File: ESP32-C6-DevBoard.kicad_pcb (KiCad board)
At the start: 2 copper layers, 63.5 x 30.5 mm, 46 parts, among them J1 USB_C_Receptacle_USB2.0_16P, J2 Conn_01x10_Pin, J3 Conn_01x10_Pin, J4 USB_C_Receptacle_USB2.0_16P, Q1 BC847, Q2 BC847, SW1 SW_Push_Dual, SW2 SW_Push_Dual, U1 ESP32-C6-MINI-1, U2 CP2104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

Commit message: First version done without autorouter.
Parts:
- removed J3: Conn_01x10_Pin, Connector_PinHeader_2.54mm:PinHeader_1x10_P2.54mm_Vertical
- removed R16: 470, Resistor_SMD:R_0603_1608Metric
- removed SW1, SW2: SW_Push_Dual, TS04_66_55_BK_260_SMT:SW_TS04-66-55-BK-260-SMT
- removed U4, U5: USBLC6-2SC6, Package_TO_SOT_SMD:SOT-23-6
- added D10: SD05_SOD323, Diode_SMD:D_SOD-323, F.Cu at (99.1, 72.4)
- added D11: SD05_SOD323, Diode_SMD:D_SOD-323, F.Cu at (100.3, 67.3)
- added D12: SD05_SOD323, Diode_SMD:D_SOD-323, F.Cu at (102.9, 72.4)
- added D8: SD05_SOD323, Diode_SMD:D_SOD-323, F.Cu at (102.9, 52.1)
- added D9: SD05_SOD323, Diode_SMD:D_SOD-323, F.Cu at (99.1, 54.6)
- added J5: Conn_01x16_Pin, Connector_PinHeader_2.54mm:PinHeader_1x16_P2.54mm_Vertical, F.Cu at (106.7, 74.9)
- added J6: Conn_01x16_Pin, Connector_PinHeader_2.54mm:PinHeader_1x16_P2.54mm_Vertical, F.Cu at (106.7, 54.6)
- added S1: TS-1088-AR02016, TS-1088-AR02016:SW_TS-1088-AR02016, F.Cu at (125.7, 59.7)
- added S2: TS-1088-AR02016, TS-1088-AR02016:SW_TS-1088-AR02016, F.Cu at (125.7, 67.3)
- C5: value 0.1uF -> 1.0uF
- D6: value LED -> SD05_SOD323; footprint LED_SMD:LED_0603_1608Metric -> Diode_SMD:D_SOD-323
- J2: value Conn_01x10_Pin -> Conn_01x02_Pin; footprint Connector_PinHeader_2.54mm:PinHeader_1x10_P2.54mm_Vertical -> Connector_PinHeader_2.54mm:PinHeader_1x02_P2.54mm_Vertical; moved to F.Cu
- moved J2 38.3 mm to (107.7, 59.3), turned to 0 degrees
- moved U3 33.0 mm to (99.1, 62.2), turned to 180 degrees
- moved D1 29.7 mm to (104.1, 59.7)
- moved R5 28.2 mm to (104.1, 62.2), turned to 0 degrees
- moved R4 25.5 mm to (101.6, 62.2), turned to 90 degrees
- moved C2 23.2 mm to (104.1, 64.8)
- moved C8 22.0 mm to (109.8, 68.6), turned to -90 degrees
- moved R3 21.6 mm to (100.3, 64.8), turned to 180 degrees
- moved C3 17.1 mm to (120.7, 67.3)
- moved C1 16.9 mm to (143.5, 57.1), turned to 0 degrees
- moved C9 15.3 mm to (111.5, 68.6), turned to -90 degrees
- moved R10 12.7 mm to (118.1, 58.4)
- moved U2 12.5 mm to (115.6, 67.3)
- moved R9 11.4 mm to (118.1, 63.5)
- moved R12 10.2 mm to (108.0, 68.6), turned to -90 degrees
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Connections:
- net /USB1_VBUS renamed /PWR_USB1_VBUS
- net /USB_5V renamed /PWR_5V
- net Net-(Q1-C) renamed /RTS
- net Net-(Q2-C) renamed /DTR
- C1 pad 1: /3V3 -> /PWR_3V3
- C2 pad 1: /3V3 -> Net-(J2-Pin_2)
- C4 pad 1: /3V3 -> /PWR_3V3
- C8 pad 1: /3V3 -> /PWR_3V3
- C9 pad 1: /3V3 -> /PWR_3V3
- D2 pad 2: /USB2_VBUS -> /PWR_USB2_VBUS
- D6 pad 2: Net-(D6-A) -> /PWR_USB2_VBUS
- J1 pad A6: Net-(J1-D+-PadA6) -> /USB1_P
- J1 pad A7: Net-(J1-D--PadA7) -> /USB1_N
- J1 pad B6: Net-(J1-D+-PadA6) -> /USB1_P
- J1 pad B7: Net-(J1-D--PadA7) -> /USB1_N
- J2 pad 1: /EIO0 -> /PWR_3V3
- J2 pad 2: /EIO1 -> Net-(J2-Pin_2)
- J4 pad A4: /USB2_VBUS -> /PWR_USB2_VBUS
- J4 pad A6: Net-(J4-D+-PadA6) -> /USB2_P
- J4 pad A7: Net-(J4-D--PadA7) -> /USB2_N
- J4 pad A9: /USB2_VBUS -> /PWR_USB2_VBUS
- J4 pad B4: /USB2_VBUS -> /PWR_USB2_VBUS
- J4 pad B6: Net-(J4-D+-PadA6) -> /USB2_P
- J4 pad B7: Net-(J4-D--PadA7) -> /USB2_N
- J4 pad B9: /USB2_VBUS -> /PWR_USB2_VBUS
- R12 pad 1: /3V3 -> /PWR_3V3
- R15 pad 1: /USB2_VBUS -> /PWR_USB2_VBUS
- R3 pad 1: /3V3 -> Net-(J2-Pin_2)
- R5 pad 1: /3V3 -> Net-(J2-Pin_2)
- R6 pad 1: /3V3 -> /PWR_3V3
- U1 pad 3: /3V3 -> /PWR_3V3
- U2 pad 5: /3V3 -> /PWR_3V3
- U2 pad 6: /3V3 -> /PWR_3V3
- U2 pad 7: /3V3 -> /PWR_3V3
- U2 pad 8: /USB2_VBUS -> /PWR_USB2_VBUS
- U3 pad 1: /3V3 -> Net-(J2-Pin_2)
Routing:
- net GND: track 313.4 -> 34.1 mm, vias 0 -> 23
- net /3V3: track 93.6 -> 0.00 mm, vias 4 -> 0
- net /PWR_3V3: track 0.00 -> 66.4 mm, vias 0 -> 2
- net /EIO0: track 61.6 -> 12.6 mm, vias 2 -> 0
- net /PWR_USB2_VBUS: track 0.00 -> 48.7 mm, vias 0 -> 2
- net /CHIP_PU: track 65.1 -> 25.0 mm, vias 2 -> 3
- net /PWR_5V: track 70.4 -> 32.3 mm, vias 3 -> 2
- net /USB2_VBUS: track 37.0 -> 0.00 mm, vias 2 -> 0
- net /ERXD0: track 51.7 -> 27.3 mm, vias 1 -> 2
- net /EIO8: track 22.8 -> 0.00 mm, vias 1 -> 0
- net /ETXD0: track 50.3 -> 28.9 mm, vias 1 -> 2
- net /EIO1: track 15.8 -> 35.2 mm
- net Net-(J4-D--PadA7): track 17.8 -> 0.00 mm, vias 2 -> 0
- net /EIO4: track 9.78 -> 26.7 mm, vias 0 -> 1
- net /USB2_N: track 16.9 -> 33.6 mm, vias 2 -> 0
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- added copper zone on B.Cu, net GND
- added copper zone on F.Cu, net GND
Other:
- board text removed: "Ekmansoft"
- board text removed: "KenTroniq"

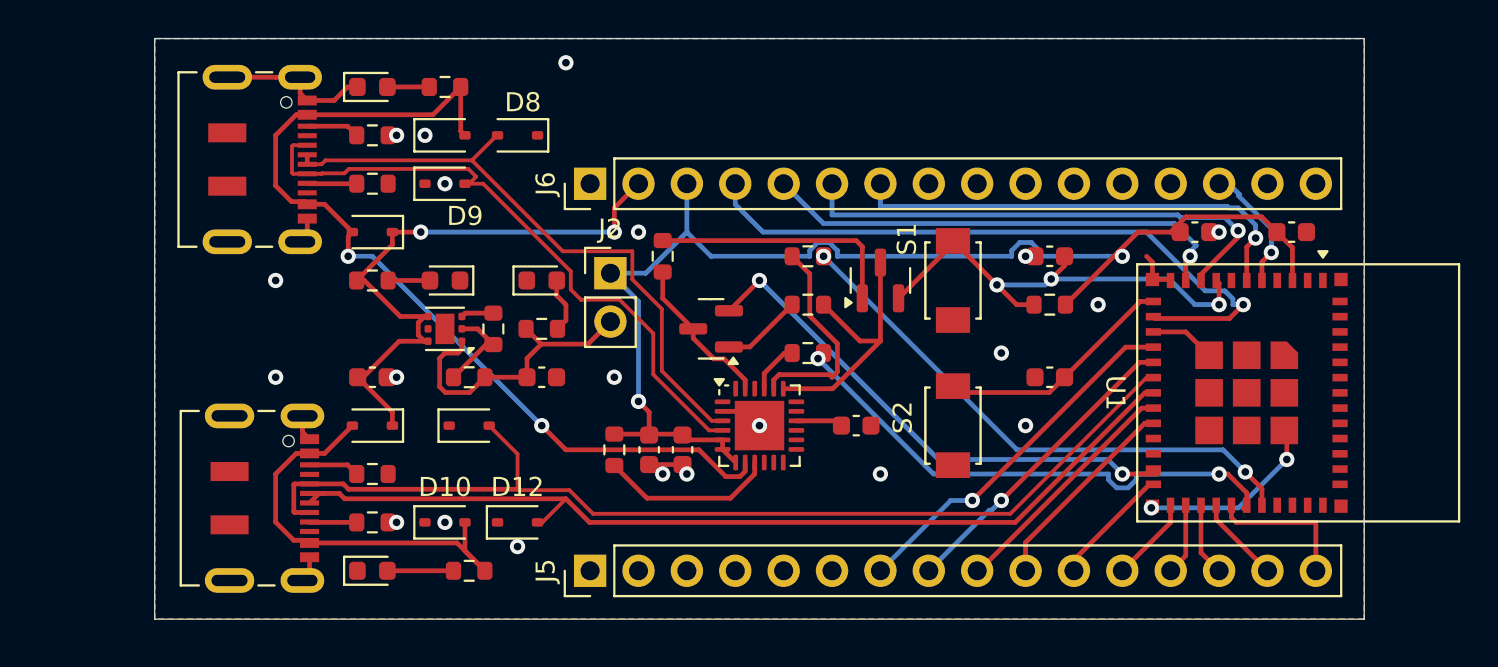
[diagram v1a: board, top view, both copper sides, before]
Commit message: Updated silk screen and corrected component error
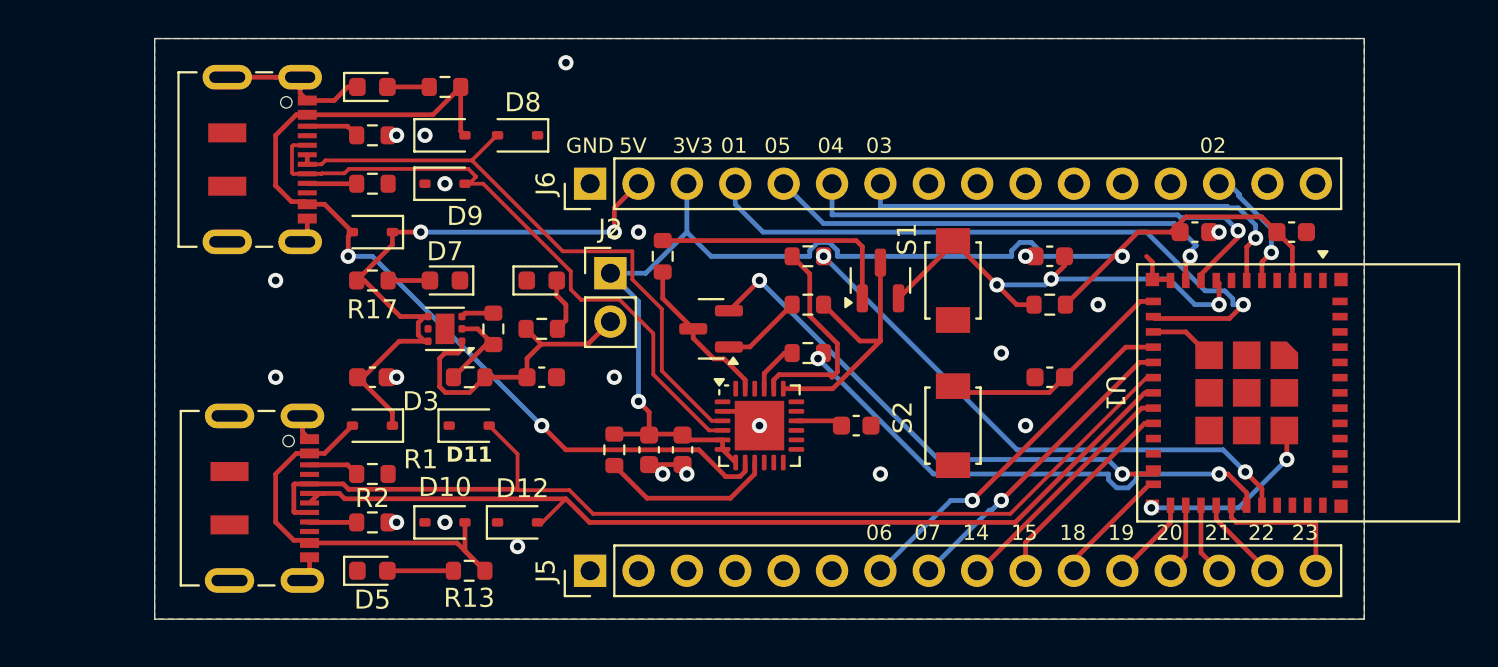
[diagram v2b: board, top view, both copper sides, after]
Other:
- board text added: "01"
- board text added: "02"
- board text added: "03"
- board text added: "04"
- board text added: "05"
- board text added: "06"
- board text added: "07"
- board text added: "14"
- board text added: "15"
- board text added: "18"
- board text added: "19"
- board text added: "20"
- board text added: "21"
- board text added: "22"
- board text added: "23"
- board text added: "3V3"
- board text added: "5V"
- board text added: "GND"
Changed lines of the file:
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@@
 		(tags "resistor")
 		(property "Reference" "R2"
-			(at 0 -1.43 0)
+			(at 0 -1.27 0)
 			(layer "F.SilkS")
-			(hide yes)
 			(effects
 				(font
@@
 		(tags "SOD-323")
 		(property "Reference" "D11"
-			(at -2.2352 -0.2794 0)
+			(at 0 1.524 0)
 			(layer "F.SilkS")
-			(hide yes)
 			(effects
 				(font
-					(size 0.4 0.4)
-					(thickness 0.06)
+					(size 0.8 0.8)
+					(thickness 0.08)
+					(bold yes)
 				)
 			)
@@
 		(tags "resistor")
 		(property "Reference" "R1"
-			(at 0 -1.43 0)
+			(at 2.54 -0.762 0)
 			(layer "F.SilkS")
-			(hide yes)
 			(effects
 				(font
@@
 		(tags "SOD-323")
 		(property "Reference" "D3"
-			(at 2.54 0.85 0)
+			(at -2.54 1.27 0)
 			(layer "F.SilkS")
-			(hide yes)
 			(effects
 				(font
@@
 		(tags "SOD-323")
 		(property "Reference" "D12"
-			(at 0 -1.85 0)
+			(at 0.254 -1.778 0)
 			(layer "F.SilkS")
 			(effects
@@
 		)
 		(fp_text user "${REFERENCE}"
-			(at 0 -1.85 0)
+			(at 0 0 0)
 			(layer "F.Fab")
 			(effects
 				(font
-					(size 1 1)
-					(thickness 0.15)
+					(size 0.4 0.4)
+					(thickness 0.06)
 				)
 			)
@@
 		(tags "LED")
 		(property "Reference" "D5"
-			(at 0 -1.43 0)
+			(at 0 1.524 0)
 			(layer "F.SilkS")
-			(hide yes)
 			(effects
 				(font
@@
 			(at 0 -1.43 0)
 			(layer "F.SilkS")
-			(hide yes)
 			(effects
 				(font
@@
 		(tags "resistor")
 		(property "Reference" "R17"
-			(at 0 -1.43 0)
+			(at 0 1.524 0)
 			(layer "F.SilkS")
-			(hide yes)
 			(effects
 				(font
@@
 		(tags "LED")
 		(property "Reference" "D7"
-			(at 0 -1.43 0)
+			(at 0 1.524 0)
 			(layer "F.SilkS")
-			(hide yes)
 			(effects
 				(font
@@
 		(layer "Edge.Cuts")
 	)
+	(gr_text "04"
+		(at 118.618 53.086 0)
+		(layer "F.SilkS")
+		(effects
+			(font
+				(size 0.8 0.8)
+				(thickness 0.1)
+			)
+			(justify left bottom)
+		)
+	)
+	(gr_text "03"
+		(at 121.158 53.086 0)
+		(layer "F.SilkS")
+		(effects
+			(font
+				(size 0.8 0.8)
+				(thickness 0.1)
+			)
+			(justify left bottom)
+		)
+	)
+	(gr_text "07"
+		(at 123.698 73.406 0)
+		(layer "F.SilkS")
+		(effects
+			(font
+				(size 0.8 0.8)
+				(thickness 0.1)
+			)
+			(justify left bottom)
+		)
+	)
+	(gr_text "15"
+		(at 128.778 73.406 0)
+		(layer "F.SilkS")
+		(effects
+			(font
+				(size 0.8 0.8)
+				(thickness 0.1)
+			)
+			(justify left bottom)
+		)
+	)
+	(gr_text "02"
+		(at 138.684 53.086 0)
+		(layer "F.SilkS")
+		(effects
+			(font
+				(size 0.8 0.8)
+				(thickness 0.1)
+			)
+			(justify left bottom)
+		)
+	)
+	(gr_text "14"
+		(at 126.238 73.406 0)
+		(layer "F.SilkS")
+		(effects
+			(font
+				(size 0.8 0.8)
+				(thickness 0.1)
+			)
+			(justify left bottom)
+		)
+	)
+	(gr_text "22"
+		(at 141.224 73.406 0)
+		(layer "F.SilkS")
+		(effects
+			(font
+				(size 0.8 0.8)
+				(thickness 0.1)
+			)
+			(justify left bottom)
+		)
+	)
+	(gr_text "3V3"
+		(at 110.998 53.086 0)
+		(layer "F.SilkS")
+		(effects
+			(font
+				(size 0.8 0.8)
+				(thickness 0.1)
+			)
+			(justify left bottom)
+		)
+	)
+	(gr_text "01"
+		(at 113.538 53.086 0)
+		(layer "F.SilkS")
+		(effects
+			(font
+				(size 0.8 0.8)
+				(thickness 0.1)
+			)
+			(justify left bottom)
+		)
+	)
+	(gr_text "5V"
+		(at 108.204 53.086 0)
+		(layer "F.SilkS")
+		(effects
+			(font
+				(size 0.8 0.8)
+				(thickness 0.1)
+			)
+			(justify left bottom)
+		)
+	)
+	(gr_text "21"
+		(at 138.938 73.406 0)
+		(layer "F.SilkS")
+		(effects
+			(font
+				(size 0.8 0.8)
+				(thickness 0.1)
+			)
+			(justify left bottom)
+		)
+	)
+	(gr_text "19"
+		(at 133.858 73.406 0)
+		(layer "F.SilkS")
+		(effects
+			(font
+				(size 0.8 0.8)
+				(thickness 0.1)
+			)
+			(justify left bottom)
+		)
+	)
+	(gr_text "23"
+		(at 143.51 73.406 0)
+		(layer "F.SilkS")
+		(effects
+			(font
+				(size 0.8 0.8)
+				(thickness 0.1)
+			)
+			(justify left bottom)
+		)
+	)
+	(gr_text "20"
+		(at 136.398 73.406 0)
+		(layer "F.SilkS")
+		(effects
+			(font
+				(size 0.8 0.8)
+				(thickness 0.1)
+			)
+			(justify left bottom)
+		)
+	)
+	(gr_text "GND"
+		(at 105.41 53.086 0)
+		(layer "F.SilkS")
+		(effects
+			(font
+				(size 0.8 0.8)
+				(thickness 0.1)
+			)
+			(justify left bottom)
+		)
+	)
+	(gr_text "06"
+		(at 121.158 73.406 0)
+		(layer "F.SilkS")
+		(effects
+			(font
+				(size 0.8 0.8)
+				(thickness 0.1)
+			)
+			(justify left bottom)
+		)
+	)
+	(gr_text "18"
+		(at 131.318 73.406 0)
+		(layer "F.SilkS")
+		(effects
+			(font
+				(size 0.8 0.8)
+				(thickness 0.1)
+			)
+			(justify left bottom)
+		)
+	)
+	(gr_text "05"
+		(at 115.824 53.086 0)
+		(layer "F.SilkS")
+		(effects
+			(font
+				(size 0.8 0.8)
+				(thickness 0.1)
+			)
+			(justify left bottom)
+		)
+	)
 	(segment

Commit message: Updated board size and 3D models
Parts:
- J5, J6: moved to B.Cu
- turned J5 to -90 degrees
- turned J6 to -90 degrees
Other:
- board size 63.5 x 30.5 mm -> 62.2 x 30.5 mm

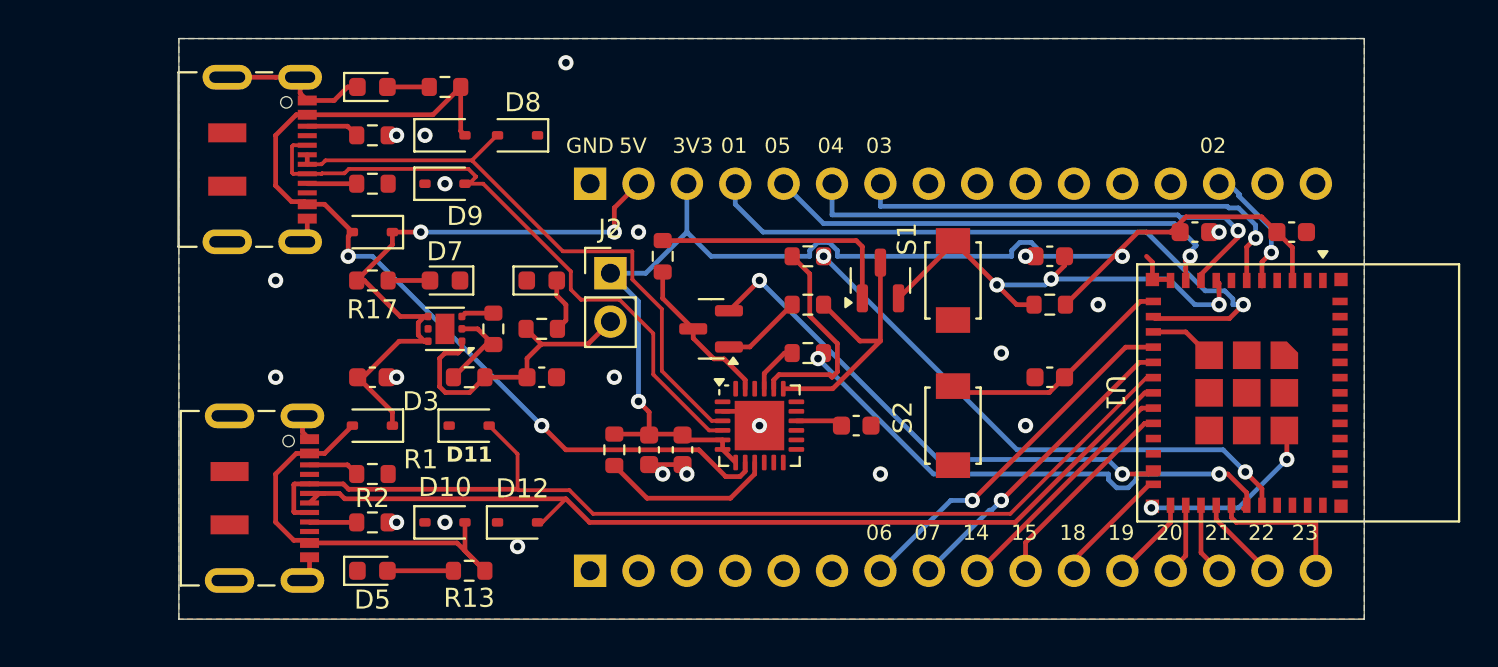
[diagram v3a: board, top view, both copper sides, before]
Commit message: Move vias placed on pads
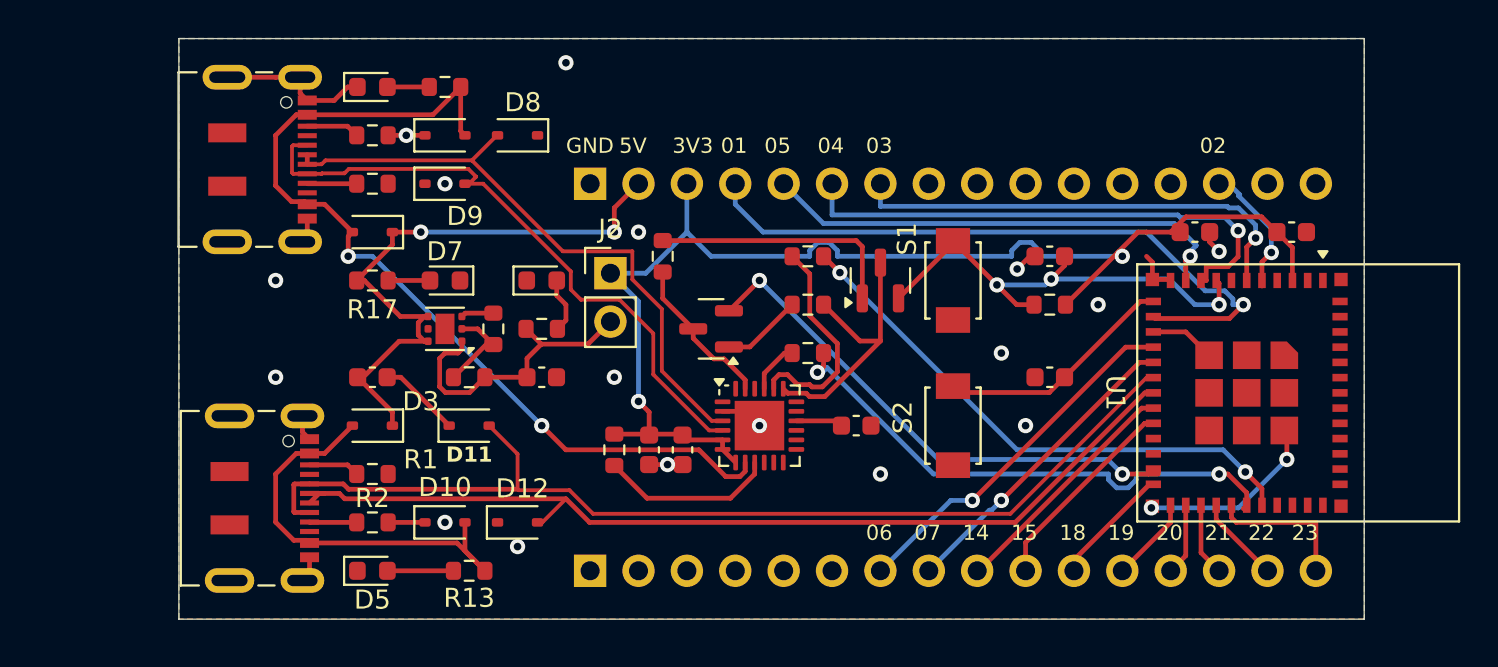
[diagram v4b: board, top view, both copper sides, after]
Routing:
- net GND: track 34.1 -> 44.7 mm, vias 23 -> 19
- net /ERXD0: track 27.3 -> 28.4 mm
- net /EIO4: track 26.7 -> 27.6 mm

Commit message: Updated BOM using Buoni kicad-jlcpcb-tools
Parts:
- D1: value LED -> LED White
- D4: value LED -> LED Red
- D5: value LED -> LED Green
- D7: value LED -> LED Yellow
